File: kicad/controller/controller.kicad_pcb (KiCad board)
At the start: 2 copper layers, 96 x 96 mm, 34 parts, among them J1 Conn_02x04_Top_Bottom, SW0 1825910-6, SW2 1825910-6, SW4 1825910-6, SW6 1825910-6, U1 MCP3008, U2 MCP23S08T-E/SO

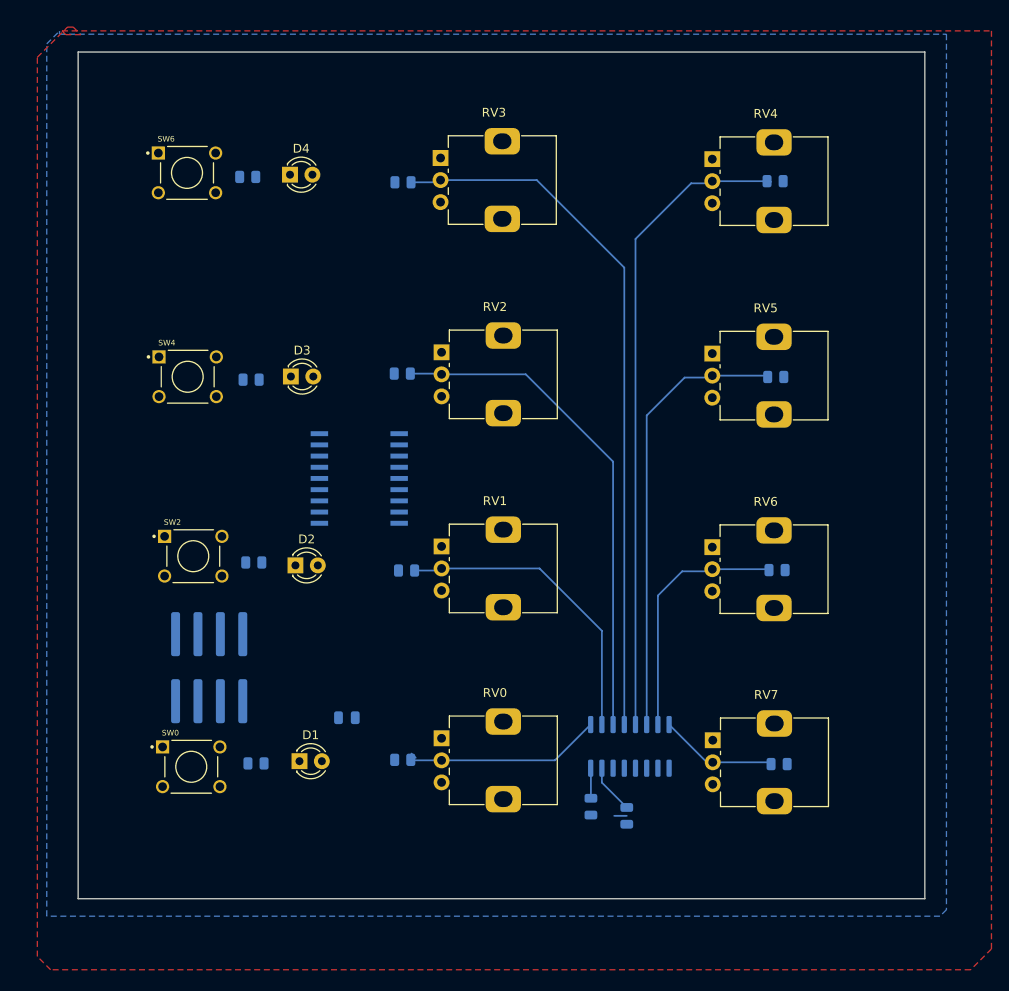
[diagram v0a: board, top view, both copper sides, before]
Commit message: tweak metronome and make a LED blink
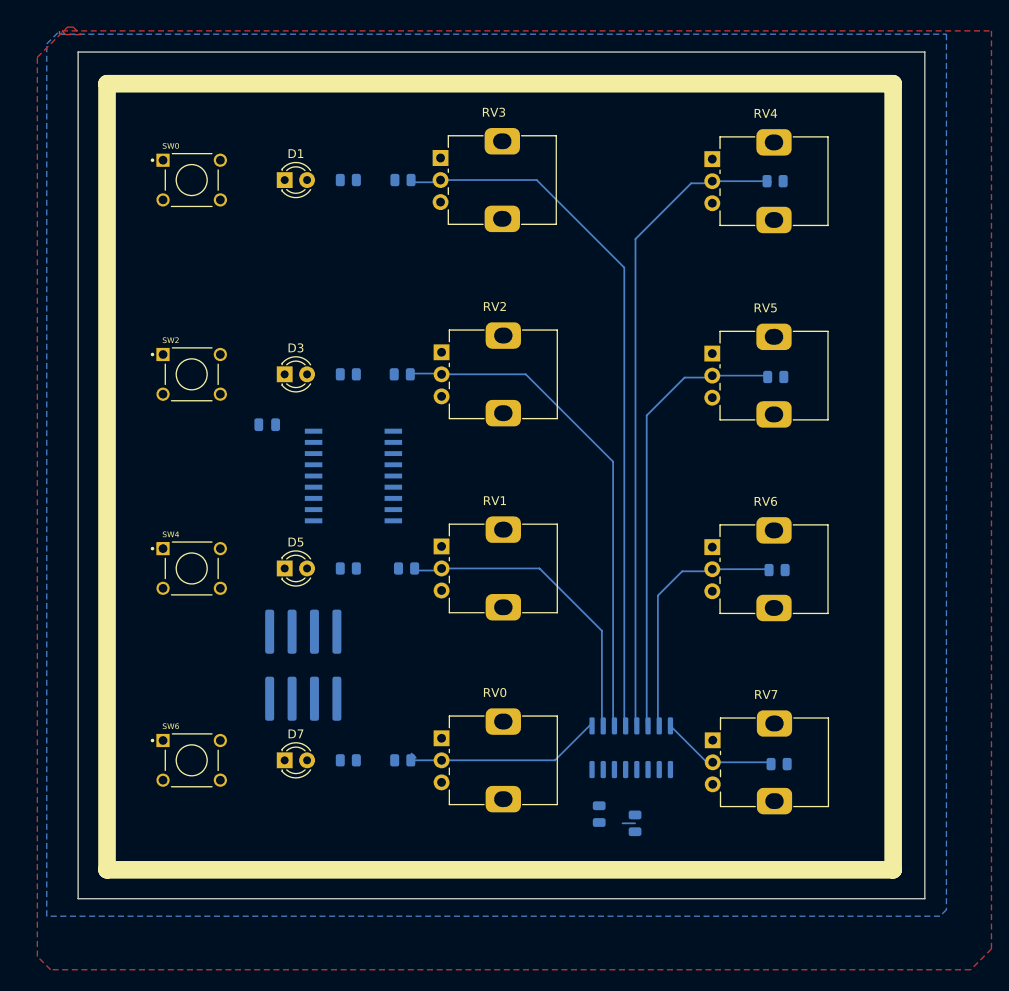
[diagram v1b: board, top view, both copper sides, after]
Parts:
- removed D2, D4: LED, LED_THT:LED_D3.0mm_FlatTop
- removed R10, R8, R9: R, Resistor_SMD:R_0805_2012Metric
- added D5: LED, LED_THT:LED_D3.0mm_FlatTop, F.Cu at (123.4, 108.6)
- added D7: LED, LED_THT:LED_D3.0mm_FlatTop, F.Cu at (123.4, 130.3)
- added R13: 2.2K, Resistor_SMD:R_0805_2012Metric, B.Cu at (130.6, 86.5)
- added R15: 2.2K, Resistor_SMD:R_0805_2012Metric, B.Cu at (130.6, 108.6)
- added R17: 2.2K, Resistor_SMD:R_0805_2012Metric, B.Cu at (130.6, 130.3)
- R11: value R -> 2.2K
- U1: value MCP3008 -> MCP23S08T-E/SO; footprint Package_SO:SOIC-16_3.9x9.9mm_P1.27mm -> Library:SOIC18-W_MC_MCH
- U2: value MCP23S08T-E/SO -> MCP3008; footprint Library:SOIC18-W_MC_MCH -> Package_SO:SOIC-16_3.9x9.9mm_P1.27mm
- moved SW6 66.6 mm to (112.9, 130.3)
- moved SW0 66.5 mm to (112.9, 64.5)
- moved D1 65.9 mm to (123.4, 64.5)
- moved U1 43.8 mm to (131.2, 98.1), turned to 180 degrees
- moved U2 43.4 mm to (162.7, 128.9), turned to -90 degrees
- moved C3 34.4 mm to (121.4, 92.3)
- moved SW4 21.7 mm to (112.9, 108.6)
- moved SW2 20.6 mm to (112.9, 86.5)
- moved R11 11.4 mm to (130.6, 64.5)
- moved J1 10.7 mm to (125.5, 119.5)
- moved C1 1.27 mm to (163.1, 137.4)
- moved C2 1.27 mm to (159.1, 136.4)
- moved D3 0.75 mm to (123.4, 86.5)
- moved R3 0.25 mm to (136.8, 64.5)
- moved R1 0.23 mm to (137.2, 108.6)
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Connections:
- C3 pad 1: unconnected-(C3-Pad1) -> GND
- C3 pad 2: unconnected-(C3-Pad2) -> +5V
- D1 pad 1: unconnected-(D1-K-Pad1) -> /GP1
- D1 pad 2: unconnected-(D1-A-Pad2) -> Net-(D1-A)
- D3 pad 1: unconnected-(D3-K-Pad1) -> /GP3
- D3 pad 2: unconnected-(D3-A-Pad2) -> Net-(D3-A)
- R11 pad 1: unconnected-(R11-Pad1) -> Net-(D1-A)
- R11 pad 2: unconnected-(R11-Pad2) -> GND
- U1 pad 1: /CH0 -> /CLK
- U1 pad 10: /CS0 -> /GP0
- U1 pad 11: /SI -> /GP1
- U1 pad 12: /SO -> /GP2
- U1 pad 13: /CLK -> /GP3
- U1 pad 14: GND -> /GP4
- U1 pad 15: +3V3 -> /GP5
- U1 pad 16: +5V -> /GP6
- U1 pad 2: /CH1 -> /SI
- U1 pad 3: /CH2 -> /SO
- U1 pad 4: /CH3 -> GND
- U1 pad 5: /CH4 -> GND
- U1 pad 6: /CH5 -> +5V
- U1 pad 7: /CH6 -> /CS1
- U1 pad 8: /CH7 -> unconnected-(U1-INT-Pad8)
- U2 pad 1: /CLK -> /CH0
- U2 pad 10: /GP0 -> /CS0
- U2 pad 11: /GP1 -> /SI
- U2 pad 12: /GP2 -> /SO
- U2 pad 13: /GP3 -> /CLK
- U2 pad 14: /GP4 -> GND
- U2 pad 15: /GP5 -> +3V3
- U2 pad 16: /GP6 -> +5V
- U2 pad 2: /SI -> /CH1
- U2 pad 3: /SO -> /CH2
- U2 pad 4: unconnected-(U2-A1-Pad4) -> /CH3
- U2 pad 5: unconnected-(U2-A0-Pad5) -> /CH4
- U2 pad 6: unconnected-(U2-*RESET-Pad6) -> /CH5
- U2 pad 7: /CS1 -> /CH6
- U2 pad 8: unconnected-(U2-INT-Pad8) -> /CH7
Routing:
- net +3V3: track 5.62 -> 0.00 mm
- net +5V: track 3.42 -> 0.03 mm

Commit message: fix button behaviour now I have a PCB
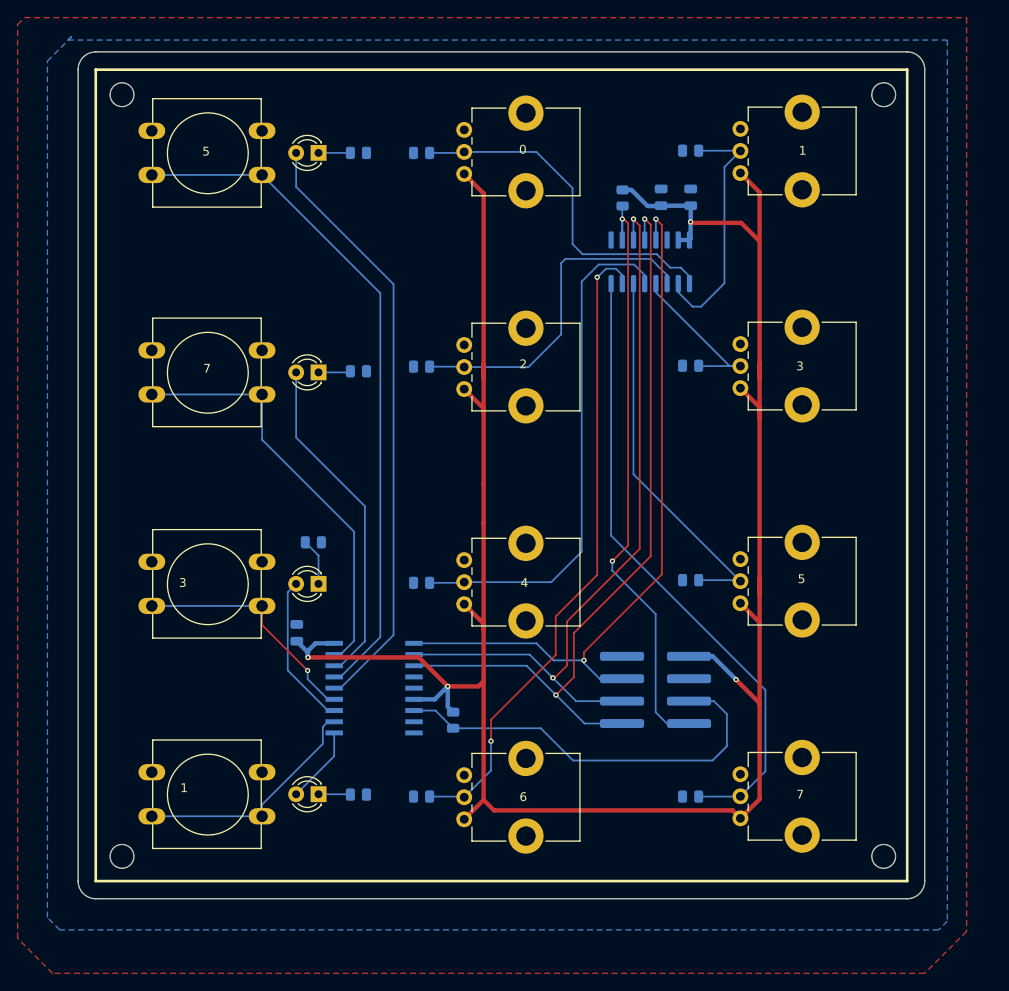
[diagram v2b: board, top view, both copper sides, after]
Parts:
- removed SW0, SW6: 1825910-6, Library:SW_1825910-6-4
- added H1: MountingHole, MountingHole:MountingHole_2.7mm_M2.5, F.Cu at (105.0, 54.8)
- added H2: MountingHole, MountingHole:MountingHole_2.7mm_M2.5, F.Cu at (105.0, 141.2)
- added H3: MountingHole, MountingHole:MountingHole_2.7mm_M2.5, F.Cu at (191.3, 141.2)
- added H4: MountingHole, MountingHole:MountingHole_2.7mm_M2.5, F.Cu at (191.3, 54.8)
- added R12: 100k, Resistor_SMD:R_0805_2012Metric, B.Cu at (161.7, 66.5)
- added R22: 100k, Resistor_SMD:R_0805_2012Metric, B.Cu at (142.5, 125.8)
- added SW1: SW_SPST, Button_Switch_THT:SW_PUSH-12mm, F.Cu at (108.4, 131.7)
- added SW5: SW_SPST, Button_Switch_THT:SW_PUSH-12mm, F.Cu at (108.4, 107.8)
- R11, R13, R15, R17: value 2.2K -> 1K
- RV0, RV1, RV2, RV3, RV4, RV5, RV6, RV7: value R_Potentiometer -> R_Pot; footprint Potentiometer_THT:Potentiometer_Alps_RK09K_Single_Vertical -> Potentiometer_THT:Potentiometer_Bourns_PTV09A-1_Single_Vertical
- SW2, SW4: value 1825910-6 -> SW_SPST; footprint Library:SW_1825910-6-4 -> Button_Switch_THT:SW_PUSH-12mm
- U1: footprint Library:SOIC18-W_MC_MCH -> Custom:SOIC18-W_MC_MCH
- moved C1 71.0 mm to (166.1, 66.5), turned to -90 degrees
- moved C2 70.7 mm to (169.5, 66.5), turned to -90 degrees
- moved D1 69.7 mm to (127.3, 134.2), turned to 180 degrees
- moved R11 69.7 mm to (131.8, 134.2), turned to 0 degrees
- moved R0 68.9 mm to (138.9, 61.4)
- moved RV0 64.0 mm to (143.8, 63.8)
- moved R4 60.7 mm to (138.9, 110.2), turned to 0 degrees
- moved RV4 57.8 mm to (143.8, 112.6)
- moved R1 57.3 mm to (169.4, 61.2)
- moved U2 55.1 mm to (164.9, 73.8), turned to 90 degrees
- moved RV1 54.2 mm to (175.1, 63.7)
- moved R6 47.8 mm to (138.9, 134.4), turned to 0 degrees
- moved D5 47.3 mm to (127.3, 61.4), turned to 180 degrees
- moved R15 47.1 mm to (131.8, 61.4), turned to 0 degrees
- moved D7 44.2 mm to (127.3, 86.3), turned to 180 degrees
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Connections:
- C2 pad 2: +5V -> +3V3
- C3 pad 2: +5V -> +3V3
- D1 pad 1: /GP1 -> Net-(D1-K)
- D1 pad 2: Net-(D1-A) -> /GP0
- D3 pad 1: /GP3 -> Net-(D3-K)
- D3 pad 2: Net-(D3-A) -> /GP2
- D5 pad 1: /GP5 -> Net-(D5-K)
- D5 pad 2: Net-(D5-A) -> /GP4
- D7 pad 1: /GP7 -> Net-(D7-K)
- D7 pad 2: Net-(D7-A) -> /GP6
- J1 pad 2: +5V -> GND
- J1 pad 4: /CS1 -> /CLK
- J1 pad 5: /CLK -> /CS1
- J1 pad 7: /SI -> /CS0
- J1 pad 8: /CS0 -> /SI
- R11 pad 1: Net-(D1-A) -> Net-(D1-K)
- R13 pad 1: Net-(D3-A) -> Net-(D3-K)
- R15 pad 1: Net-(D5-A) -> Net-(D5-K)
- R17 pad 1: Net-(D7-A) -> Net-(D7-K)
- RV0 pad 1: GND -> +3V3
- RV0 pad 3: +3V3 -> GND
- RV1 pad 1: GND -> +3V3
- RV1 pad 3: +3V3 -> GND
- RV2 pad 1: GND -> +3V3
- RV2 pad 3: +3V3 -> GND
- RV3 pad 1: GND -> +3V3
- RV3 pad 3: +3V3 -> GND
- RV4 pad 1: GND -> +3V3
- RV4 pad 3: +3V3 -> GND
- RV5 pad 1: GND -> +3V3
- RV5 pad 3: +3V3 -> GND
- RV6 pad 1: GND -> +3V3
- RV6 pad 3: +3V3 -> GND
- RV7 pad 1: GND -> +3V3
- RV7 pad 3: +3V3 -> GND
- SW2 pad 1: /GP2 -> GND
- SW2 pad 2: unconnected-(SW2-Pad2) -> /GP5
- SW4 pad 1: /GP4 -> GND
- SW4 pad 2: unconnected-(SW4-Pad2) -> /GP7
- U1 pad 18: +5V -> +3V3
- U1 pad 2: /SI -> /SO
- U1 pad 3: /SO -> /SI
- U1 pad 6: +5V -> +3V3
- U2 pad 11: /SI -> /SO
- U2 pad 12: /SO -> /SI
- U2 pad 16: +5V -> +3V3
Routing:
- net +3V3: track 0.00 -> 268.9 mm, vias 0 -> 4
- net /SI: track 0.00 -> 87.5 mm, vias 0 -> 2
- net /SO: track 0.00 -> 84.6 mm, vias 0 -> 2
- net /CLK: track 0.00 -> 81.8 mm, vias 0 -> 2
- net /GP5: track 0.00 -> 77.6 mm
- net /CS0: track 0.00 -> 70.0 mm, vias 0 -> 2
- net /GP4: track 0.00 -> 68.5 mm
- net /CH3: track 80.9 -> 18.8 mm
- net /CH7: track 13.4 -> 71.3 mm
- net /GP7: track 0.00 -> 47.7 mm
- net /CS1: track 0.00 -> 47.0 mm
- net /CH6: track 28.2 -> 73.7 mm, vias 0 -> 2
- net /GP6: track 0.00 -> 38.3 mm
- net /GP3: track 0.00 -> 27.5 mm, vias 0 -> 1
- net /GP1: track 0.00 -> 27.3 mm
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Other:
- outline, holes or cut-outs redrawn
- board text added: "0"
- board text added: "1"
- board text added: "2"
- board text added: "3"
- board text added: "4"
- board text added: "5"
- board text added: "6"
- board text added: "7"
- board text added: "TOP"
- board text removed: "board is 96x96 to keep within the cheap tier of pcbway"

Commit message: fiddling with the config as I test the PCB
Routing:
- net /GP7: track 47.7 -> 35.2 mm
- net /GP3: track 27.5 -> 15.0 mm
- net /GP5: track 77.6 -> 65.1 mm
- net /GP1: track 27.3 -> 14.8 mm
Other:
- board text added: "button 7 and 5 are awkward"
- board text added: "reroute maybe swap order of button and led? sideset +1"
- board text added: "still want a low pass filter on buttons just RC and that's it"

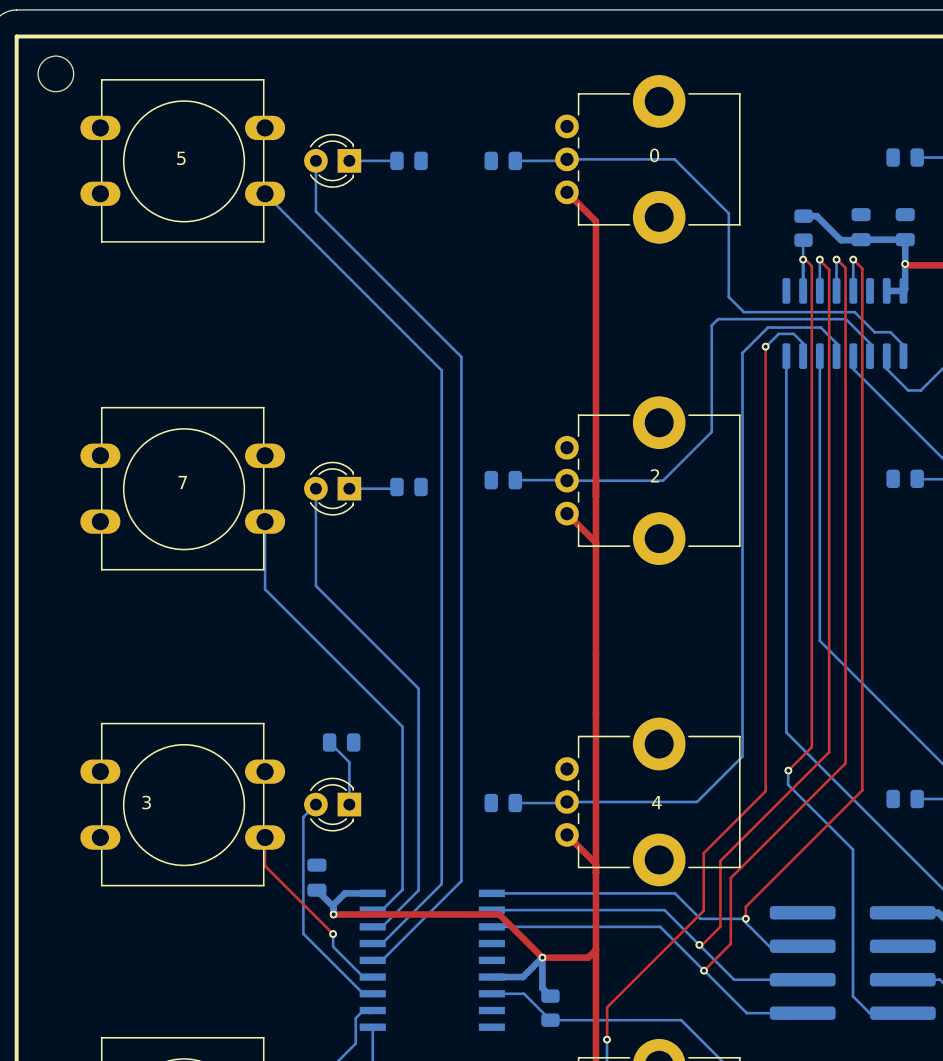
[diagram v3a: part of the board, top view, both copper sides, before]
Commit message: removed debounce as in practice it did not help
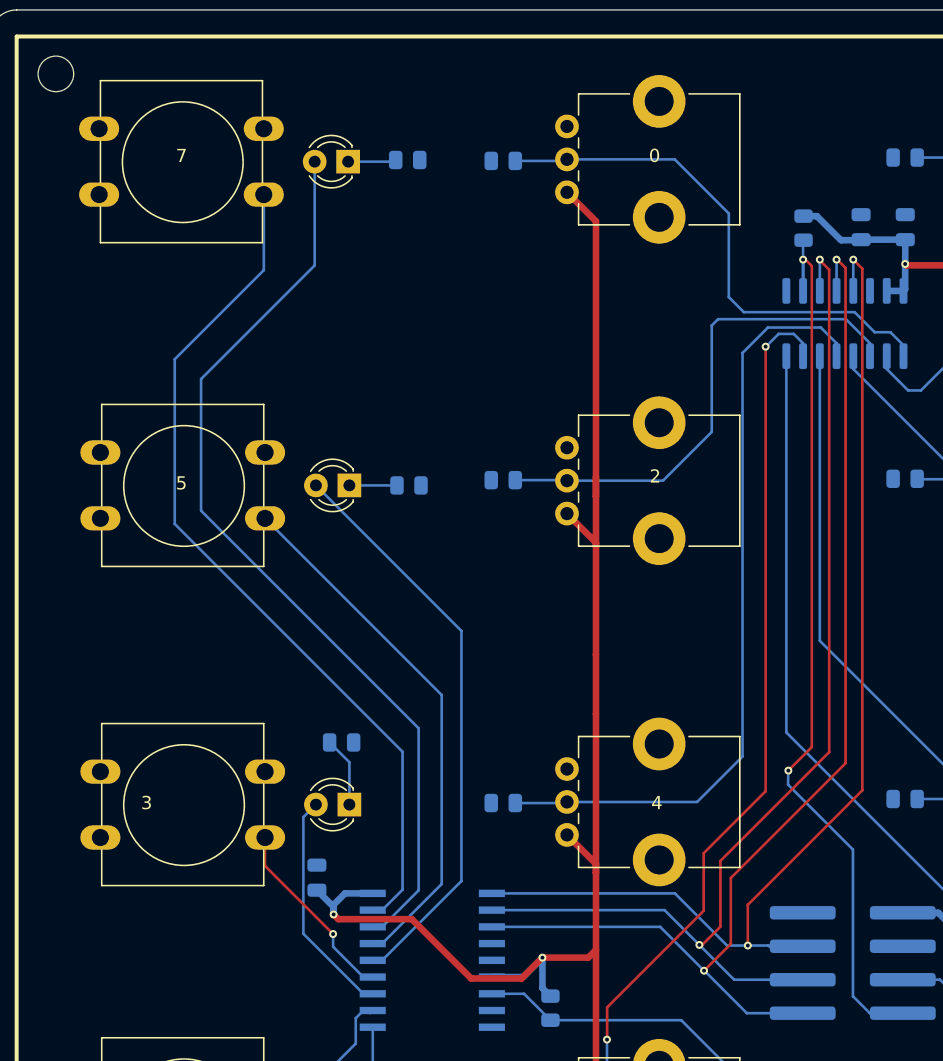
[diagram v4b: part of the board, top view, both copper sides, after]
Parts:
- moved D7 24.8 mm to (127.2, 61.5)
- moved SW4 24.8 mm to (108.3, 59.0)
- moved R17 24.8 mm to (131.7, 61.4)
- moved D5 24.6 mm to (127.3, 86.1)
- moved R15 24.6 mm to (131.8, 86.1)
- moved SW2 24.6 mm to (108.4, 83.6)
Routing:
- net /GP6: track 38.3 -> 70.4 mm
- net /GP7: track 35.2 -> 65.6 mm
- net /GP5: track 65.1 -> 40.4 mm
- net /GP4: track 68.5 -> 43.8 mm
- net /CLK: track 81.8 -> 83.6 mm
- net +3V3: track 268.9 -> 270.2 mm
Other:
- board text removed: "button 7 and 5 are awkward"
- board text removed: "reroute maybe swap order of button and led? sideset +1"
- board text removed: "still want a low pass filter on buttons just RC and that's it"
